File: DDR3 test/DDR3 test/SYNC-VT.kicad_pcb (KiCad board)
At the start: 6 copper layers, 65 x 30 mm, 69 parts, among them U1 MPM3834CGPA-Z, U2 MPM3834CGPA-Z, U3 XC7Z010-1CLG225I, U4 TPS3106K33DBVR, U5 W25Q128JVS, U6 0473092651, U7 S80KS5123GABHA020, U8 S80KS5123GABHA020, X1 SIT8008BI-73-XXS-33.333333

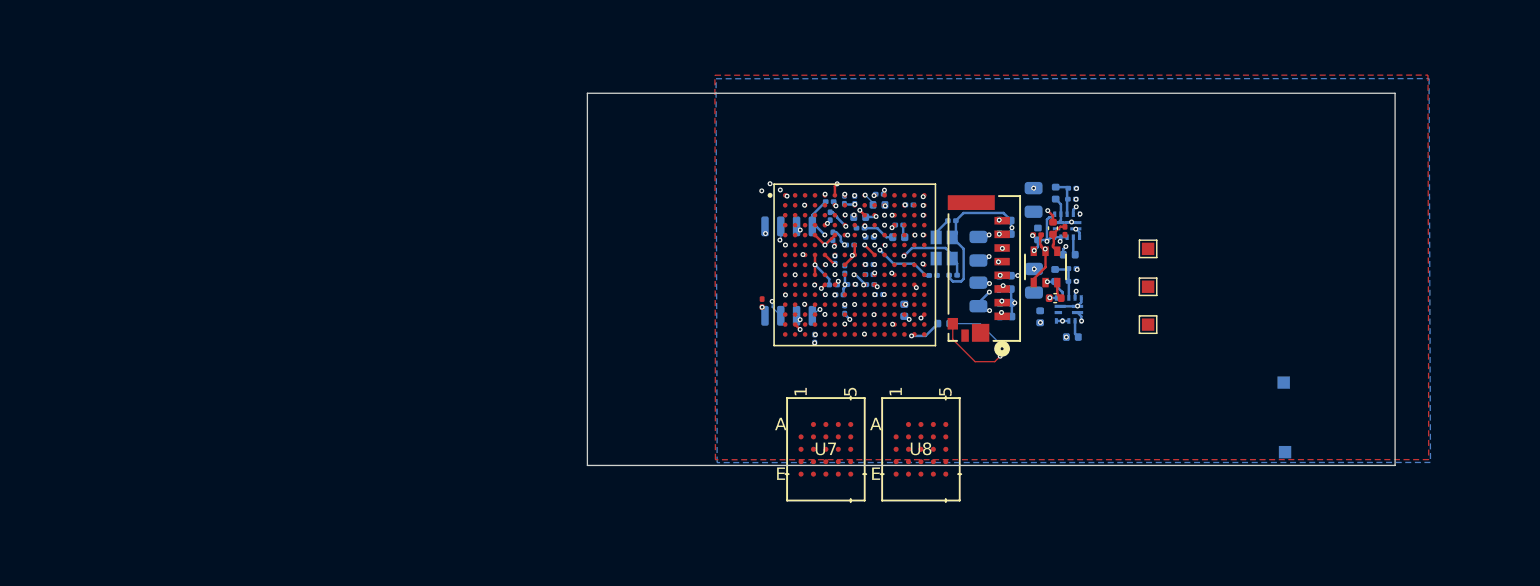
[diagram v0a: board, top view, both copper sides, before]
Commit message: group ddr pins by function in symbol
group ddr pins by function in symbol
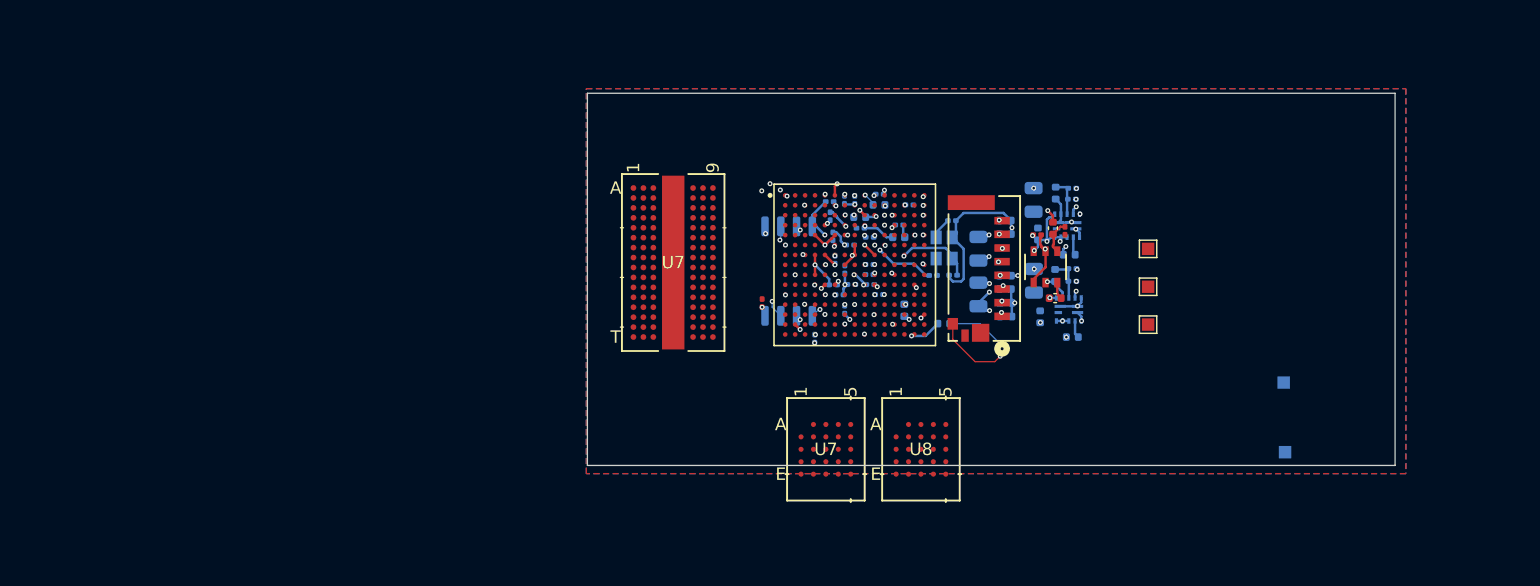
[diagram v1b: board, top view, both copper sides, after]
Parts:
- added U7: MT41K256M16TW-107:P, footprint:FBGA96_8X14_MRN, F.Cu at (86.0, 49.0)
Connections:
- U3 pad J13: RAM_DQ5 -> unconnected-(U3B-IO_L5P_T0_34-PadJ13)
- U3 pad K12: ~{RAM_CS0} -> unconnected-(U3B-IO_L11N_T1_SRCC_34-PadK12)
- U3 pad K13: RAM_DQ0 -> unconnected-(U3B-IO_L10P_T1_34-PadK13)
- U3 pad L12: ~{RAM_RST} -> unconnected-(U3B-IO_L12P_T1_MRCC_34-PadL12)
- U3 pad L13: RAM_DQ6 -> unconnected-(U3B-IO_L10N_T1_34-PadL13)
- U3 pad L14: RAM_DQ4 -> unconnected-(U3B-IO_L9P_T1_DQS_34-PadL14)
- U3 pad L15: RAM_CLK -> unconnected-(U3B-IO_L8P_T1_34-PadL15)
- U3 pad M14: RWDS -> unconnected-(U3B-IO_L9N_T1_DQS_34-PadM14)
- U3 pad M15: ~{RAM_CLK} -> unconnected-(U3B-IO_L8N_T1_34-PadM15)
- U3 pad N11: RAM_DQ1 -> unconnected-(U3B-IO_L13P_T2_MRCC_34-PadN11)
- U3 pad N14: RAM_DQ2 -> unconnected-(U3B-IO_L7N_T1_34-PadN14)
- U3 pad P11: RAM_DQ7 -> unconnected-(U3B-IO_L16P_T2_34-PadP11)
- U3 pad P14: RAM_DQ3 -> unconnected-(U3B-IO_L18N_T2_34-PadP14)
- U3 pad R10: ~{RAM_CS1} -> unconnected-(U3B-IO_L24N_T3_34-PadR10)

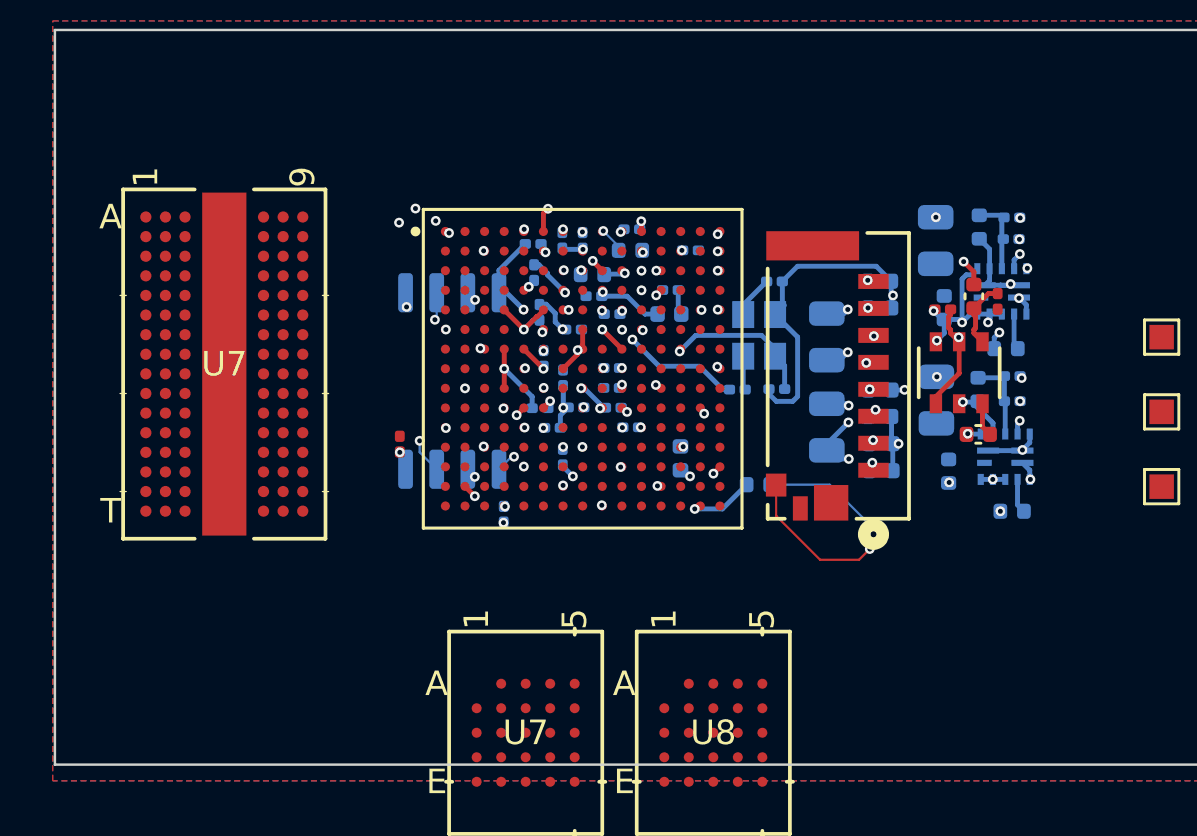
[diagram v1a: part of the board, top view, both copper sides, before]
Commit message: Resistor Footprints
- Fixed resistor footprints
- Re-added 3D models
- Routed 1.5V reg
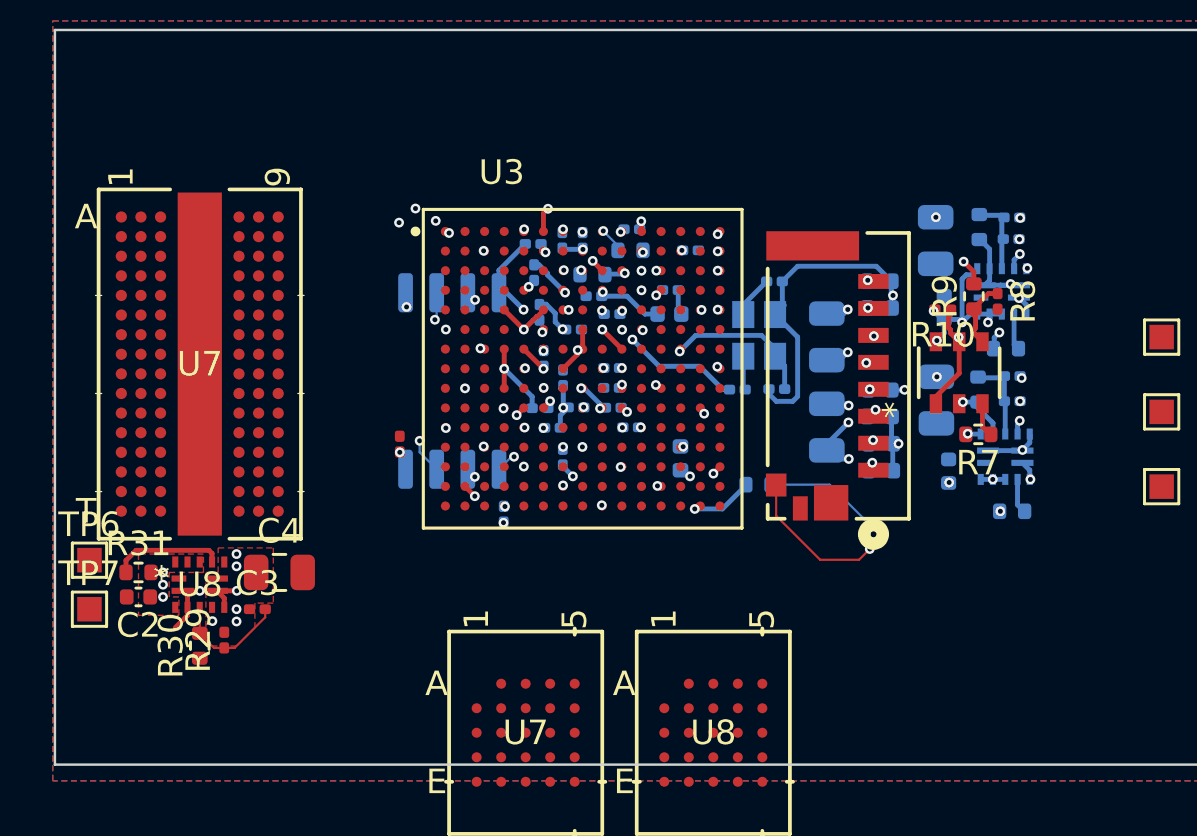
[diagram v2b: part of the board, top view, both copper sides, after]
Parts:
- added C2: 22uF, Capacitor_SMD:C_0402_1005Metric, F.Cu at (82.5, 58.5)
- added C3: 10pF, Capacitor_SMD:C_0201_0603Metric, F.Cu at (87.3, 59.0)
- added C4: 47uF, Capacitor_SMD:C_0805_2012Metric, F.Cu at (88.2, 57.5)
- added R29: 20k, Resistor_SMD:R_0201_0603Metric, F.Cu at (86.0, 60.3)
- added R30: 13.3k, Resistor_SMD:R_0402_1005Metric, F.Cu at (85.0, 60.5)
- added R31: 10k, Resistor_SMD:R_0402_1005Metric, F.Cu at (82.5, 57.5)
- added TP6: TP, TestPoint:TestPoint_Pad_1.0x1.0mm, F.Cu at (80.5, 57.0)
- added TP7: TP, TestPoint:TestPoint_Pad_1.0x1.0mm, F.Cu at (80.5, 59.0)
- added U8: MPM3834CGPA-Z, Sync_VT extras:ECLGA-14_MPM3834C_MNP, F.Cu at (85.0, 58.0)
- R1, R10, R11, R12, R13, R14, R15, R16, R17, R20, R21, R22, R3, R8: footprint Capacitor_SMD:C_0201_0603Metric -> Resistor_SMD:R_0201_0603Metric
- R18, R19, R2, R23, R24, R25, R26, R27, R28, R4, R5, R6, R7, R9: footprint Capacitor_SMD:C_0402_1005Metric -> Resistor_SMD:R_0402_1005Metric
- U3: footprint Sync_VT extras:225-LFBGA -> Sync_VT extras:BGA225C80P15X15_1300X1300X150N
- U7: footprint footprint:FBGA96_8X14_MRN -> Sync_VT extras:FBGA96_8X14_MRN
- moved U7 1.00 mm to (85.0, 49.0)
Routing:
- net Net-(U8-FB): track 0.00 -> 4.83 mm
- net GND: track 26.2 -> 31.0 mm, vias 35 -> 37
- net Net-(TP6-Pin_1): track 0.00 -> 4.57 mm
- net +3V3: vias 28 -> 31
- net +1V5: vias 0 -> 5
- added copper zone on F.Cu, net +1V5
- added copper zone on F.Cu, net +3V3

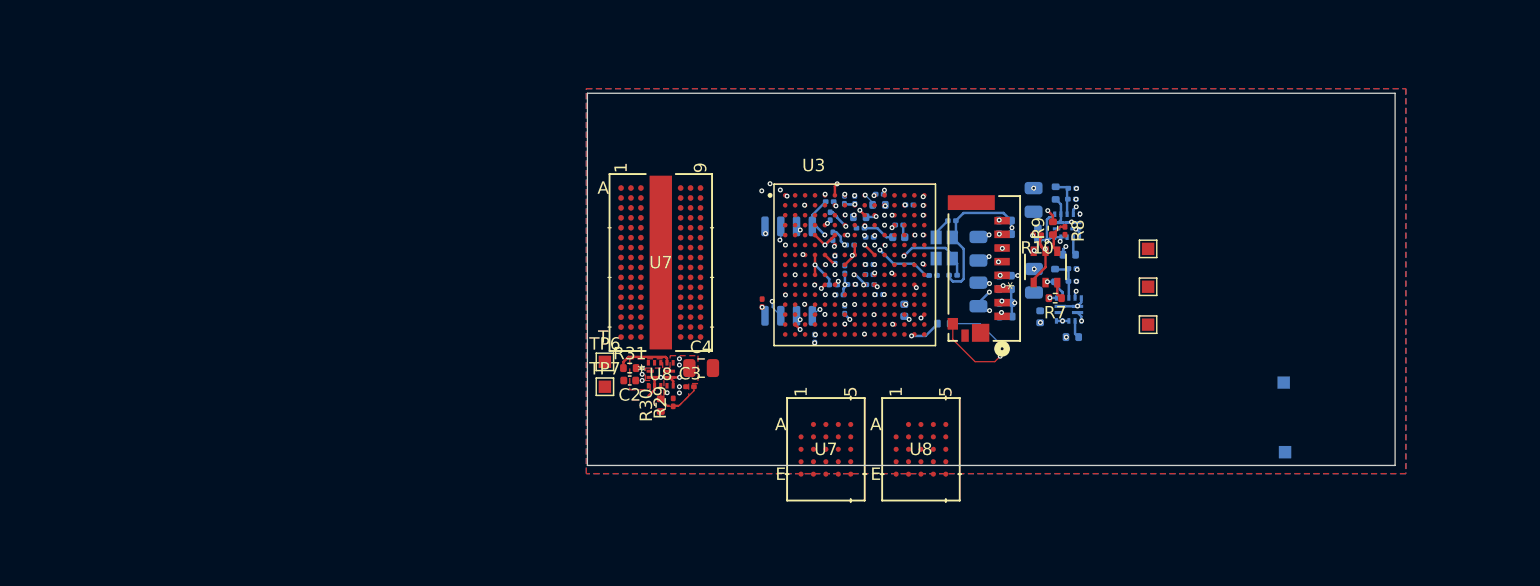
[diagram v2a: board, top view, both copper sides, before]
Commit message: BGA fanned out
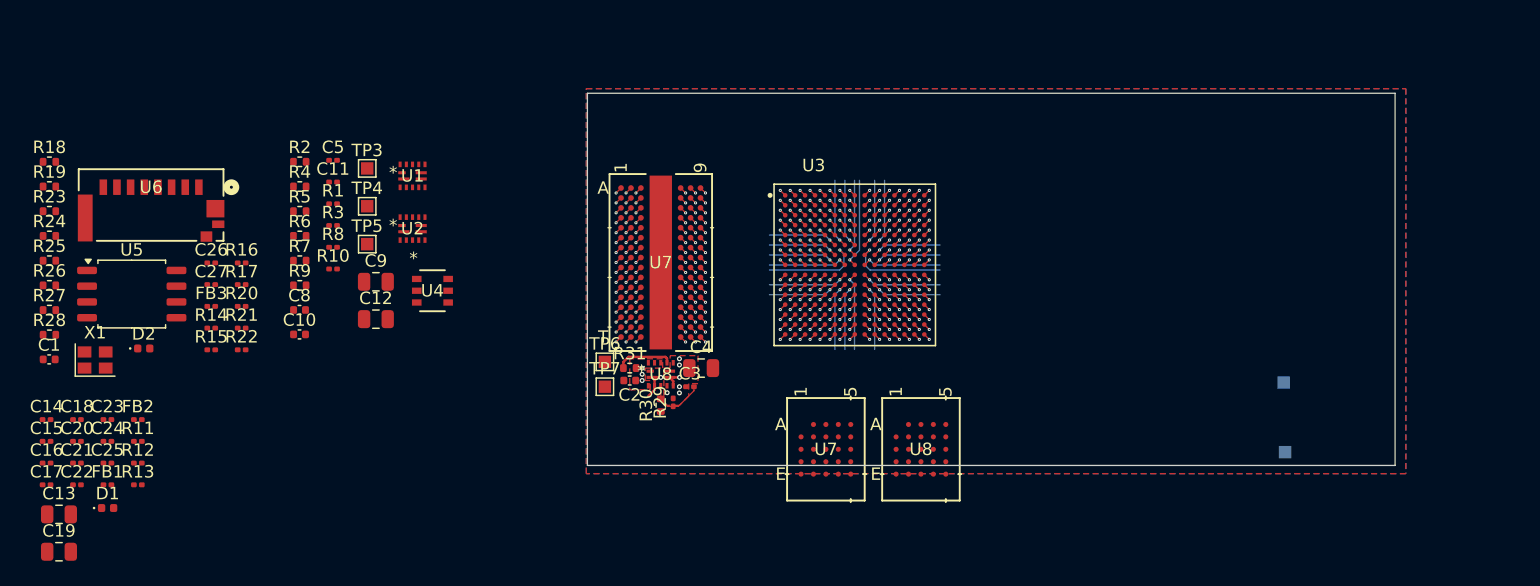
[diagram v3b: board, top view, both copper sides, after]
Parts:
- C1, C10, C11, C12, C13, C14, C15, C16, C17, C18, C19, C20, C21, C22, C23, C24, C25, C27, C5, C8, C9, D1, D2, FB1, FB2, FB3, R1, R11, R12, R13, R14, R15, R16, R17, R18, R19, R2, R20, R21, R22, R23, R24, R25, R26, R27, R28, R3, R4, R5, R6, U1, U2, U5, X1: moved to F.Cu
- moved C19 78.0 mm to (36.5, 72.3), turned to 0 degrees
- moved R28 77.5 mm to (35.8, 54.8), turned to 0 degrees
- moved C1 77.3 mm to (35.8, 56.8)
- moved R24 77.3 mm to (35.8, 46.9), turned to 0 degrees
- moved R27 77.2 mm to (35.8, 52.8), turned to 0 degrees
- moved R25 77.1 mm to (35.8, 48.9), turned to 0 degrees
- moved R26 77.0 mm to (35.8, 50.8), turned to 0 degrees
- moved C13 76.1 mm to (36.5, 69.3), turned to 0 degrees
- moved R23 72.6 mm to (35.8, 44.9)
- moved X1 69.0 mm to (39.5, 56.9), turned to 0 degrees
- moved C25 67.8 mm to (40.4, 65.2)
- moved C15 67.8 mm to (35.5, 63.4)
- moved U6 67.3 mm to (44.0, 44.4), turned to 0 degrees
- moved C14 67.2 mm to (35.5, 61.6)
- moved R19 66.8 mm to (35.8, 42.9), turned to 0 degrees
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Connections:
- U3 pad A2: unconnected-(U3E-PS_DDR_DQ1_502-PadA2) -> /RAM/DDR4_DQ1
- U3 pad A3: unconnected-(U3E-PS_DDR_DQ7_502-PadA3) -> /RAM/DDR4_DQ7
- U3 pad A4: unconnected-(U3E-PS_DDR_DQ5_502-PadA4) -> /RAM/DDR4_DQ5
- U3 pad B4: unconnected-(U3E-PS_DDR_DQ4_502-PadB4) -> /RAM/DDR4_DQ4
- U3 pad C1: unconnected-(U3E-PS_DDR_DQ3_502-PadC1) -> /RAM/DDR4_DQ3
- U3 pad C3: unconnected-(U3E-PS_DDR_DQ6_502-PadC3) -> /RAM/DDR4_DQ6
- U3 pad C4: unconnected-(U3E-PS_DDR_DQ2_502-PadC4) -> /RAM/DDR4_DQ2
- U3 pad D1: unconnected-(U3E-PS_DDR_DQ9_502-PadD1) -> /RAM/DDR4_DQ9
- U3 pad D4: unconnected-(U3E-PS_DDR_DQ0_502-PadD4) -> /RAM/DDR4_DQ0
- U3 pad E1: unconnected-(U3E-PS_DDR_DQ8_502-PadE1) -> /RAM/DDR4_DQ8
- U3 pad E2: unconnected-(U3E-PS_DDR_DQ10_502-PadE2) -> /RAM/DDR4_DQ10
- U3 pad E3: unconnected-(U3E-PS_DDR_DQ11_502-PadE3) -> /RAM/DDR4_DQ11
- U3 pad F3: unconnected-(U3E-PS_DDR_DQ12_502-PadF3) -> /RAM/DDR4_DQ12
- U3 pad G1: unconnected-(U3E-PS_DDR_DQ13_502-PadG1) -> /RAM/DDR4_DQ13
- U3 pad H1: unconnected-(U3E-PS_DDR_DQ14_502-PadH1) -> /RAM/DDR4_DQ14
- U3 pad H2: unconnected-(U3E-PS_DDR_DQ15_502-PadH2) -> /RAM/DDR4_DQ15
- U3 pad J1: unconnected-(U3E-PS_DDR_A10_502-PadJ1) -> /RAM/DDR4_A10
- U3 pad K1: unconnected-(U3E-PS_DDR_A14_502-PadK1) -> /RAM/DDR4_A14
- U3 pad K2: unconnected-(U3E-PS_DDR_A13_502-PadK2) -> /RAM/DDR4_A13
- U3 pad L2: unconnected-(U3E-PS_DDR_A11_502-PadL2) -> /RAM/DDR4_A11
- U3 pad M1: unconnected-(U3E-PS_DDR_A2_502-PadM1) -> /RAM/DDR4_A2
- U3 pad M2: unconnected-(U3E-PS_DDR_A12_502-PadM2) -> /RAM/DDR4_A12
- U3 pad M4: unconnected-(U3E-PS_DDR_A3_502-PadM4) -> /RAM/DDR4_A3
- U3 pad M5: unconnected-(U3E-PS_DDR_A7_502-PadM5) -> /RAM/DDR4_A7
- U3 pad N1: unconnected-(U3E-PS_DDR_A1_502-PadN1) -> /RAM/DDR4_A1
- U3 pad N4: unconnected-(U3E-PS_DDR_A9_502-PadN4) -> /RAM/DDR4_A9
- U3 pad P1: unconnected-(U3E-PS_DDR_A0_502-PadP1) -> /RAM/DDR4_A0
- U3 pad P3: unconnected-(U3E-PS_DDR_A4_502-PadP3) -> /RAM/DDR4_A4
- U3 pad P4: unconnected-(U3E-PS_DDR_A5_502-PadP4) -> /RAM/DDR4_A5
- U3 pad P5: unconnected-(U3E-PS_DDR_A6_502-PadP5) -> /RAM/DDR4_A6
- U3 pad P6: unconnected-(U3E-PS_DDR_A8_502-PadP6) -> /RAM/DDR4_A8
- U7 pad A2: unconnected-(U7-DQ13-PadA2) -> /RAM/DDR4_DQ13
- U7 pad A3: unconnected-(U7-DQ15-PadA3) -> /RAM/DDR4_DQ15
- U7 pad A7: unconnected-(U7-DQ12-PadA7) -> /RAM/DDR4_DQ12
- U7 pad B8: unconnected-(U7-DQ14-PadB8) -> /RAM/DDR4_DQ14
- U7 pad C2: unconnected-(U7-DQ11-PadC2) -> /RAM/DDR4_DQ11
- U7 pad C3: unconnected-(U7-DQ9-PadC3) -> /RAM/DDR4_DQ9
- U7 pad C8: unconnected-(U7-DQ10-PadC8) -> /RAM/DDR4_DQ10
- U7 pad D7: unconnected-(U7-DQ8-PadD7) -> /RAM/DDR4_DQ8
- U7 pad E3: unconnected-(U7-DQ0-PadE3) -> /RAM/DDR4_DQ0
- U7 pad F2: unconnected-(U7-DQ2-PadF2) -> /RAM/DDR4_DQ2
- U7 pad F7: unconnected-(U7-DQ1-PadF7) -> /RAM/DDR4_DQ1
- U7 pad F8: unconnected-(U7-DQ3-PadF8) -> /RAM/DDR4_DQ3
- U7 pad G2: unconnected-(U7-DQ6-PadG2) -> /RAM/DDR4_DQ6
- U7 pad H3: unconnected-(U7-DQ4-PadH3) -> /RAM/DDR4_DQ4
- U7 pad H7: unconnected-(U7-DQ7-PadH7) -> /RAM/DDR4_DQ7
- U7 pad H8: unconnected-(U7-DQ5-PadH8) -> /RAM/DDR4_DQ5
- U7 pad L7: unconnected-(U7-A10/AP-PadL7) -> /RAM/DDR4_A10
- U7 pad N2: unconnected-(U7-A3-PadN2) -> /RAM/DDR4_A3
- U7 pad N3: unconnected-(U7-A0-PadN3) -> /RAM/DDR4_A0
- U7 pad N7: unconnected-(U7-A12/*BC-PadN7) -> /RAM/DDR4_A12
- U7 pad P2: unconnected-(U7-A5-PadP2) -> /RAM/DDR4_A5
- U7 pad P3: unconnected-(U7-A2-PadP3) -> /RAM/DDR4_A2
- U7 pad P7: unconnected-(U7-A1-PadP7) -> /RAM/DDR4_A1
- U7 pad P8: unconnected-(U7-A4-PadP8) -> /RAM/DDR4_A4
- U7 pad R2: unconnected-(U7-A7-PadR2) -> /RAM/DDR4_A7
- U7 pad R3: unconnected-(U7-A9-PadR3) -> /RAM/DDR4_A9
- U7 pad R7: unconnected-(U7-A11-PadR7) -> /RAM/DDR4_A11
- U7 pad R8: unconnected-(U7-A6-PadR8) -> /RAM/DDR4_A6
- U7 pad T3: unconnected-(U7-A13-PadT3) -> /RAM/DDR4_A13
- U7 pad T7: unconnected-(U7-A14-PadT7) -> /RAM/DDR4_A14
- U7 pad T8: unconnected-(U7-A8-PadT8) -> /RAM/DDR4_A8
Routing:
- net GND: track 31.0 -> 124.9 mm, vias 37 -> 34
- net +1V8: track 7.45 -> 52.9 mm, vias 18 -> 13
- net +1V0: track 11.6 -> 41.4 mm, vias 14 -> 8
- net +3V3: track 35.2 -> 61.5 mm, vias 31 -> 21
- net SPI-CLK: track 21.1 -> 1.38 mm, vias 3 -> 1
- net SPI-D3: track 20.9 -> 1.38 mm, vias 3 -> 1
- net POR_B: track 24.0 -> 5.72 mm, vias 2 -> 1
- net GNDA: track 1.93 -> 18.3 mm, vias 1 -> 3
- net MIO29: track 16.5 -> 3.94 mm, vias 2 -> 1
- net Net-(R23-Pad2): track 11.7 -> 0.00 mm, vias 1 -> 0
- net SPI-D0: track 12.7 -> 1.38 mm, vias 2 -> 1
- net SPI-D1: track 10.6 -> 1.38 mm, vias 3 -> 1
- net MIO30: track 9.75 -> 1.44 mm, vias 2 -> 1
- net unconnected-(U3A-VP_0-PadG7): track 0.00 -> 8.10 mm, vias 0 -> 1
- net unconnected-(U3A-TCK_0-PadG9): track 0.00 -> 8.10 mm, vias 0 -> 1
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- added copper zone on In3.Cu, net GND
- removed copper zone on In1.Cu, net +1V0
- removed copper zone on In1.Cu, net +1V8
- removed copper zone on In3.Cu, net +3V3
